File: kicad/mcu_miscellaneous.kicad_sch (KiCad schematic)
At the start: 10 parts, among them SW1 SW_Push, SW2 SW_Push

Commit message: fix(schematic): misc. fixes and stuff - sort all sheets - add the author's name to all sheets and update the date - add 0R resistor to the input of each crystal oscillator - reannotate all symbols - remove todo.md
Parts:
- renumbered C17 to C16, C16 to C17, D3 to D2, R7 to R3, R2 to R4, R1 to R5, R9 to R6
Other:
- moved on the sheet: C16, C17, D1, D2, R3, R4, R5, R6, SW1, SW2

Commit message: everything: select real components, refactor schematic, add a user-led driving circuit, and more
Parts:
- added Q1: NPN, symbol Simulation_SPICE:NPN
- added R13, R16: 5k1, Resistor_SMD:R_0402_1005Metric, symbol Device:R
- C16, C17: footprint (none) -> Capacitor_SMD:C_0402_1005Metric; Distributor (none) -> LCSC; Distributor Link (none) -> https://www.lcsc.com/product-detail/C60474.html?s_z=s_p_CC0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; MPN (none) -> CC0402KRX7R7BB104; Manufacturer (none) -> YAGEO
- D1: footprint (none) -> LED_SMD:LED_0402_1005Metric; Distributor (none) -> LCSC; Distributor Link (none) -> https://www.lcsc.com/product-detail/C511042.html?s_z=s_p_VL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; MPN (none) -> VLMB1500-GS08; Manufacturer (none) -> VISHAY
- D2: Distributor (none) -> LCSC; MPN (none) -> BAT54KFILM; Manufacturer Part Number BAT54KFILM -> (none)
- R3: value 220R -> 0R; footprint (none) -> Resistor_SMD:R_0402_1005Metric
- R4, R5, R6: footprint (none) -> Resistor_SMD:R_0402_1005Metric
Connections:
- net +3V3: now also D1.2 (A)
- net GND: now also Q1.3 (E), R16.1; no longer R3.2
- net USER_LED: now also R13.1; no longer D1.2 (A)
- new net: Q1.1 (C), R3.2
- new net: Q1.2 (B), R13.2, R16.2
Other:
- note added: "Blue LED, Has a high V_F. and 3V3 will let about 10 mA of current. and my STM32 won't like that."
- note added: "maybe this can act as a fuse?"
- note added: "this is placed to prevent leakage current from turning the transistor on spontaneously. similar to MOSFETs I guess.... But I think I need to make it a bit smaller, not very small though, or the NPN wont turn on. Making it smaller in LTSpice (2N2222) to around 500 ohms made it unable to achieve saturation. and the resistor will also conduct too much current. so, if not carefully, this is a double 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"
- moved on the sheet: C16, C17, D1, D2, R3, R4, R5, R6, SW1, SW2

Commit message: feat(components): add details
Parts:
- D1: value LED -> VLMB1500-GS08
- SW1, SW2: value SW_Push -> B3U-1000P; Distributor (none) -> LCSC; Distributor Link (none) -> https://www.lcsc.com/product-detail/C231329.html?spm=wm.fly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; MPN (none) -> B3U-1000P; Manufacturer (none) -> OMRON
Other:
- note added: "verify footprint"
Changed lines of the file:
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@@
+		)
+	)
+	(text "verify footprint"
+		(exclude_from_sim no)
+		(at 110.49 115.57 0)
+		(effects
+			(font
+				(size 1.27 1.27)
+			)
 		)
 	)
@@
 			)
 		)
-		(property "Value" "SW_Push"
+		(property "Value" "B3U-1000P"
 			(at 162.56 99.0599 90)
 			(show_name no)
@@
 			)
 		)
-		(property "Datasheet" ""
+		(property "Datasheet" "https://www.lcsc.com/datasheet/C231329.pdf?spm=wm.sxq.inf.ggs___wm.fly.bg.2.xh&lcsc_vid=RlRYUFFURFcNVFIDFVMMXgZSRlJeUABSQVNfAwJfQwIxVlNeTlZeVlJfTlNaVDtW"
 			(at 156.21 97.79 0)
 			(hide yes)
@@
 			)
 		)
-		(property "Description" "Push button switch, generic, two pins"
+		(property "Description" "SWITCH TACTILE SPST 153gf SMD"
 			(at 161.29 97.79 0)
 			(hide yes)
@@
 			)
 		)
-		(property "Distributor Link" ""
+		(property "Distributor Link" "https://www.lcsc.com/product-detail/C231329.html?spm=wm.fly.bg.2.xh___wm.fly.tp.20.ml&lcsc_vid=RlRYUFFURFcNVFIDFVMMXgZSRlJeUABSQVNfAwJfQwIxVlNeTlZeVlJfTlNaVDtW"
 			(at 161.29 97.79 90)
 			(hide yes)
@@
 			)
 		)
-		(property "Manufacturer" ""
+		(property "Manufacturer" "OMRON"
 			(at 161.29 97.79 90)
 			(hide yes)
@@
 			)
 		)
-		(property "Distributor" ""
+		(property "Distributor" "LCSC"
+			(at 161.29 97.79 90)
+			(hide yes)
+			(show_name no)
+			(do_not_autoplace no)
+			(effects
+				(font
+					(size 1.27 1.27)
+				)
+			)
+		)
+		(property "MPN" "B3U-1000P"
 			(at 161.29 97.79 90)
 			(hide yes)
@@
 			)
 		)
-		(property "Value" "SW_Push"
+		(property "Value" "B3U-1000P"
 			(at 217.17 110.4899 90)
 			(show_name no)
@@
 			)
 		)
-		(property "Datasheet" ""
+		(property "Datasheet" "https://www.lcsc.com/datasheet/C231329.pdf?spm=wm.sxq.inf.ggs___wm.fly.bg.2.xh&lcsc_vid=RlRYUFFURFcNVFIDFVMMXgZSRlJeUABSQVNfAwJfQwIxVlNeTlZeVlJfTlNaVDtW"
 			(at 210.82 109.22 0)
 			(hide yes)
@@
 			)
 		)
-		(property "Description" "Push button switch, generic, two pins"
+		(property "Description" "SWITCH TACTILE SPST 153gf SMD"
 			(at 215.9 109.22 0)
 			(hide yes)
@@
 			)
 		)
-		(property "Distributor Link" ""
+		(property "Distributor Link" "https://www.lcsc.com/product-detail/C231329.html?spm=wm.fly.bg.2.xh___wm.fly.tp.20.ml&lcsc_vid=RlRYUFFURFcNVFIDFVMMXgZSRlJeUABSQVNfAwJfQwIxVlNeTlZeVlJfTlNaVDtW"
 			(at 215.9 109.22 90)
 			(hide yes)
@@
 			)
 		)
-		(property "Manufacturer" ""
+		(property "Manufacturer" "OMRON"
 			(at 215.9 109.22 90)
 			(hide yes)
@@
 			)
 		)
-		(property "Distributor" ""
+		(property "Distributor" "LCSC"
+			(at 215.9 109.22 90)
+			(hide yes)
+			(show_name no)
+			(do_not_autoplace no)
+			(effects
+				(font
+					(size 1.27 1.27)
+				)
+			)
+		)
+		(property "MPN" "B3U-1000P"
 			(at 215.9 109.22 90)
 			(hide yes)
@@
 			)
 		)
-		(property "Value" "LED"
+		(property "Value" "VLMB1500-GS08"
 			(at 99.06 87.9474 90)
 			(show_name no)

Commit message: fix(footprints and symbols): add missing footprints and symbols
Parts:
- removed Q1: NPN, symbol Simulation_SPICE:NPN
- removed SW1, SW2: B3U-1000P, symbol Switch:SW_Push
- added Q1: S9013-E, Package_TO_SOT_SMD:SOT-23, symbol #stm32-bt-board-external-symbols:S9013-E
- added SW1, SW2: B3U-1000P, #stm32-bt-board-external-footprints:B3U-1000P, symbol #stm32-bt-board-external-symbols:B3U-1000P
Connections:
- net +3V3: now also SW1.2
- net GND: now also Q1.2 (E), SW2.1
- net NRST_IN: now also SW2.2
- net at R3.2: now also Q1.3 (C)
- net at R13.2, R16.2: now also Q1.1 (B)
- net at R4.1: now also SW1.1
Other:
- note removed: "verify footprint"

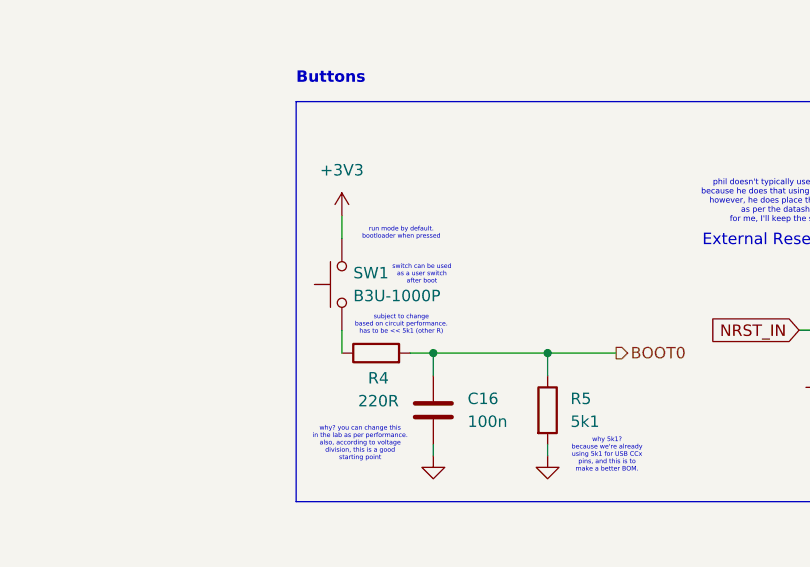
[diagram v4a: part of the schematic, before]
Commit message: refactor(schematic): flip SW1 so layout is nicer
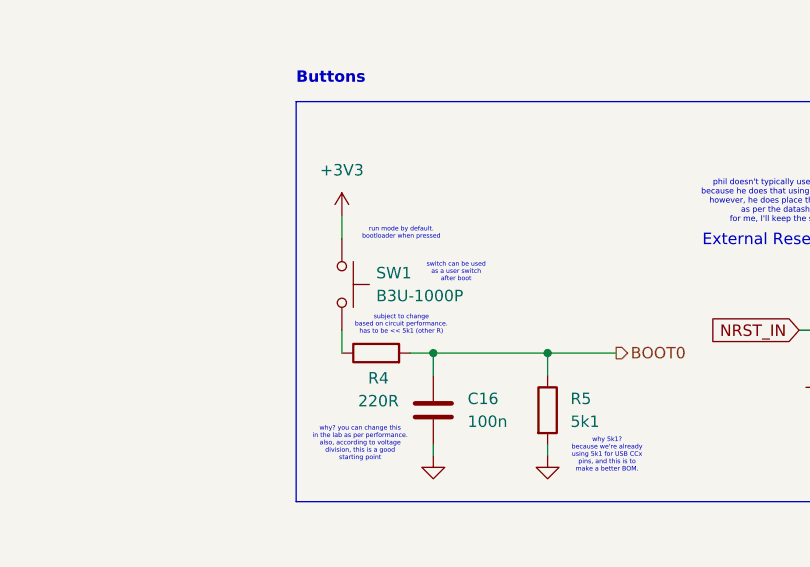
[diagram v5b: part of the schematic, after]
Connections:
- net +3V3: now also SW1.1; no longer SW1.2
- net at R4.1: now also SW1.2; no longer SW1.1
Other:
- moved on the sheet: SW1
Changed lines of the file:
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@@
 	(text "switch can be used\nas a user switch\nafter boot"
 		(exclude_from_sim no)
-		(at 170.18 96.774 0)
+		(at 173.99 96.52 0)
 		(effects
 			(font
@@
 	(symbol
 		(lib_id "#stm32-bt-board-external-symbols:B3U-1000P")
-		(at 161.29 97.79 90)
+		(at 161.29 97.79 270)
 		(unit 1)
 		(body_style 1)
@@
 		(fields_autoplaced yes)
 		(property "Reference" "SW1"
-			(at 162.56 96.5199 90)
-			(show_name no)
-			(do_not_autoplace no)
-			(effects
-				(font
-					(size 1.27 1.27)
-				)
-				(justify right)
+			(at 165.1 96.5199 90)
+			(show_name no)
+			(do_not_autoplace no)
+			(effects
+				(font
+					(size 1.27 1.27)
+				)
+				(justify left)
 			)
 		)
 		(property "Value" "B3U-1000P"
-			(at 162.56 99.0599 90)
-			(show_name no)
-			(do_not_autoplace no)
-			(effects
-				(font
-					(size 1.27 1.27)
-				)
-				(justify right)
+			(at 165.1 99.0599 90)
+			(show_name no)
+			(do_not_autoplace no)
+			(effects
+				(font
+					(size 1.27 1.27)
+				)
+				(justify left)
 			)
 		)
 		(property "Footprint" "#stm32-bt-board-external-footprints:B3U-1000P"
-			(at 156.21 97.79 0)
+			(at 166.37 97.79 0)
 			(hide yes)
 			(show_name no)
@@
 		)
 		(property "Datasheet" "https://www.lcsc.com/datasheet/C231329.pdf?spm=wm.sxq.inf.ggs___wm.fly.bg.0.xh&lcsc_vid=RlRYUFFURFcNVFIDFVMMXgZSRlJeUABSQVNfAwJfQwIxVlNeTllXUlNQR1dcUzsOAxUeFF5JWBYZEEoKFBINSQcJGk4eFQsCAgIaSgADAwAHC0slRFBXUFJeQ08GEwkK"
-			(at 156.21 97.79 0)
-			(hide yes)
-			(show_name no)
+			(at 166.37 97.79 0)
+			(hide yes)
+			(show_name no)

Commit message: feat(BOM): fill missing parts in BOM
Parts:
- R13, R16, R5: Distributor (none) -> LCSC; Distributor Link (none) -> https://www.lcsc.com/product-detail/C105872.html; MPN (none) -> RC0402FR-075K1L; Manufacturer (none) -> YAGEO
- R3: Distributor (none) -> LCSC; Distributor Link (none) -> https://www.lcsc.com/product-detail/C190119.html; MPN (none) -> CRCW04020000Z0ED; Manufacturer (none) -> VISHAY
- R4: Distributor (none) -> LCSC; Distributor Link (none) -> https://www.lcsc.com/product-detail/C2909336.html; MPN (none) -> FRC0402F2200TS; Manufacturer (none) -> FOJAN
- R6: Distributor (none) -> LCSC; Distributor Link (none) -> https://www.lcsc.com/product-detail/C60491.html; MPN (none) -> RC0402FR-07100KL; Manufacturer (none) -> YAGEO
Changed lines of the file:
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@@
 			)
 		)
-		(property "Datasheet" ""
+		(property "Datasheet" "https://www.lcsc.com/datasheet/C105872.pdf"
 			(at 184.15 111.76 0)
 			(hide yes)
@@
 			)
 		)
-		(property "Description" "-- mixed values --"
+		(property "Description" "RES 5.1kΩ ±1% 62.5mW 0402"
 			(at 184.15 111.76 0)
 			(hide yes)
@@
 			)
 		)
-		(property "Distributor Link" ""
+		(property "Distributor Link" "https://www.lcsc.com/product-detail/C105872.html"
 			(at 184.15 111.76 0)
 			(hide yes)
@@
 			)
 		)
-		(property "Manufacturer" ""
+		(property "Manufacturer" "YAGEO"
 			(at 184.15 111.76 0)
 			(hide yes)
@@
 			)
 		)
-		(property "Distributor" ""
+		(property "Distributor" "LCSC"
+			(at 184.15 111.76 0)
+			(hide yes)
+			(show_name no)
+			(do_not_autoplace no)
+			(effects
+				(font
+					(size 1.27 1.27)
+				)
+			)
+		)
+		(property "MPN" "RC0402FR-075K1L"
 			(at 184.15 111.76 0)
 			(hide yes)
@@
 			)
 		)
-		(property "Datasheet" ""
+		(property "Datasheet" "https://www.lcsc.com/datasheet/C105872.pdf"
 			(at 83.82 121.92 0)
 			(hide yes)
@@
 			)
 		)
-		(property "Description" "Resistor"
+		(property "Description" "RES 5.1kΩ ±1% 62.5mW 0402"
+			(at 83.82 121.92 0)
+			(hide yes)
+			(show_name no)
+			(do_not_autoplace no)
+			(effects
+				(font
+					(size 1.27 1.27)
+				)
+			)
+		)
+		(property "Distributor" "LCSC"
+			(at 83.82 121.92 0)
+			(hide yes)
+			(show_name no)
+			(do_not_autoplace no)
+			(effects
+				(font
+					(size 1.27 1.27)
+				)
+			)
+		)
+		(property "Distributor Link" "https://www.lcsc.com/product-detail/C105872.html"
+			(at 83.82 121.92 0)
+			(hide yes)
+			(show_name no)
+			(do_not_autoplace no)
+			(effects
+				(font
+					(size 1.27 1.27)
+				)
+			)
+		)
+		(property "MPN" "RC0402FR-075K1L"
+			(at 83.82 121.92 0)
+			(hide yes)
+			(show_name no)
+			(do_not_autoplace no)
+			(effects
+				(font
+					(size 1.27 1.27)
+				)
+			)
+		)
+		(property "Manufacturer" "YAGEO"
 			(at 83.82 121.92 0)
 			(hide yes)
@@
 			)
 		)
-		(property "Datasheet" ""
+		(property "Datasheet" "https://www.lcsc.com/datasheet/C190119.pdf"
 			(at 95.25 104.14 0)
 			(hide yes)
@@
 			)
 		)
-		(property "Description" "Resistor"
+		(property "Description" "RES 0Ω 62.5mW 0402"
 			(at 95.25 104.14 0)
 			(hide yes)
@@
 			)
 		)
-		(property "Distributor Link" ""
+		(property "Distributor Link" "https://www.lcsc.com/product-detail/C190119.html"
 			(at 95.25 104.14 0)
 			(hide yes)
@@
 			)
 		)
-		(property "Manufacturer" ""
+		(property "Manufacturer" "VISHAY"
 			(at 95.25 104.14 0)
 			(hide yes)
@@
 			)
 		)
-		(property "Distributor" ""
+		(property "Distributor" "LCSC"
+			(at 95.25 104.14 0)
+			(hide yes)
+			(show_name no)
+			(do_not_autoplace no)
+			(effects
+				(font
+					(size 1.27 1.27)
+				)
+			)
+		)
+		(property "MPN" "CRCW04020000Z0ED"
 			(at 95.25 104.14 0)
 			(hide yes)
@@
 			)
 		)
-		(property "Datasheet" ""
+		(property "Datasheet" "https://www.lcsc.com/datasheet/C2909336.pdf"
 			(at 165.1 105.41 0)
 			(hide yes)
@@
 			)
 		)
-		(property "Description" "Resistor"
+		(property "Description" "RES 220Ω ±1% 62.5mW 0402"
 			(at 165.1 105.41 0)
 			(hide yes)
@@
 			)
 		)
-		(property "Distributor Link" ""
+		(property "Distributor Link" "https://www.lcsc.com/product-detail/C2909336.html"
 			(at 165.1 105.41 90)
 			(hide yes)
@@
 			)
 		)
-		(property "Manufacturer" ""
+		(property "Manufacturer" "FOJAN"
 			(at 165.1 105.41 90)
 			(hide yes)
@@
 			)
 		)
-		(property "Distributor" ""
+		(property "Distributor" "LCSC"
+			(at 165.1 105.41 90)
+			(hide yes)
+			(show_name no)
+			(do_not_autoplace no)
+			(effects
+				(font
+					(size 1.27 1.27)
+				)
+			)
+		)
+		(property "MPN" "FRC0402F2200TS"
 			(at 165.1 105.41 90)
 			(hide yes)
@@
 			)
 		)
-		(property "Datasheet" ""
+		(property "Datasheet" "https://www.lcsc.com/datasheet/C60491.pdf"
 			(at 250.19 96.52 0)
 			(hide yes)
@@
 			)
 		)
-		(property "Description" "Resistor"
+		(property "Description" "RES 100kΩ ±1% 62.5mW 0402"
 			(at 250.19 96.52 0)
 			(hide yes)
@@
 			)
 		)
-		(property "Distributor" ""
+		(property "Distributor" "LCSC"
+			(at 250.19 96.52 0)
+			(hide yes)
+			(show_name no)
+			(do_not_autoplace no)
+			(effects
+				(font
+					(size 1.27 1.27)
+				)
+			)
+		)
+		(property "Distributor Link" "https://www.lcsc.com/product-detail/C60491.html"
+			(at 250.19 96.52 0)
+			(hide yes)
+			(show_name no)
+			(do_not_autoplace no)
+			(effects
+				(font
+					(size 1.27 1.27)
+				)
+			)
+		)
+		(property "MPN" "RC0402FR-07100KL"
+			(at 250.19 96.52 0)
+			(hide yes)
+			(show_name no)
+			(do_not_autoplace no)
+			(effects
+				(font
+					(size 1.27 1.27)
+				)
+			)
+		)
+		(property "Manufacturer" "YAGEO"
 			(at 250.19 96.52 0)
 			(hide yes)
@@
 			)
 		)
-		(property "Datasheet" ""
+		(property "Datasheet" "https://www.lcsc.com/datasheet/C105872.pdf"
 			(at 73.66 115.57 0)
 			(hide yes)
@@
 			)
 		)
-		(property "Description" "Resistor"
+		(property "Description" "RES 5.1kΩ ±1% 62.5mW 0402"
 			(at 73.66 115.57 0)
 			(hide yes)
 			(show_name no)
+			(do_not_autoplace no)
+			(effects
+				(font
+					(size 1.27 1.27)
+				)
+			)
+		)
+		(property "Distributor" "LCSC"
+			(at 73.66 115.57 90)
+			(hide yes)
+			(show_name no)
+			(do_not_autoplace no)
+			(effects
+				(font
+					(size 1.27 1.27)
+				)
+			)
+		)
+		(property "Distributor Link" "https://www.lcsc.com/product-detail/C105872.html"
+			(at 73.66 115.57 90)
+			(hide yes)
+			(show_name no)
+			(do_not_autoplace no)
+			(effects
+				(font
+					(size 1.27 1.27)
+				)
+			)
+		)
+		(property "MPN" "RC0402FR-075K1L"
+			(at 73.66 115.57 90)
+			(hide yes)
+			(show_name no)
+			(do_not_autoplace no)
+			(effects
+				(font
+					(size 1.27 1.27)
+				)
+			)
+		)
+		(property "Manufacturer" "YAGEO"
+			(at 73.66 115.57 90)
+			(hide yes)
+			(show_name no)

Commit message: feat(manuf.): edit BOM and CPL to match JLCPCB's requirements
however, please pay close attention to the rotations during ordering, especially for the SOT components, as JLCPCB messes them up a bit, same for the connector and the filter
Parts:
- C16, C17: Distributor Link https://www.lcsc.com/product-detail/C60474.html?s_z=s_p_CC0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 -> https://www.lcsc.com/product-detail/C60474.html; JLCPCB Part # (none) -> C60474
- D1: Distributor Link https://www.lcsc.com/product-detail/C511042.html?s_z=s_p_VL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 -> https://www.lcsc.com/product-detail/C511042.html; JLCPCB Part # (none) -> C511042
- D2: Distributor Link https://www.lcsc.com/product-detail/C283259.html?s_z=s_p_BA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 -> https://www.lcsc.com/product-detail/C283259.html; JLCPCB Part # (none) -> C283259
- Q1: Distributor Link https://www.lcsc.com/product-detail/C41371419.html?s_z=h_q_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 -> https://www.lcsc.com/product-detail/C41371419.html; JLCPCB Part # (none) -> C41371419
- R13, R16, R5: JLCPCB Part # (none) -> C105872
- R3: JLCPCB Part # (none) -> C190119
- R4: JLCPCB Part # (none) -> C2909336
- R6: JLCPCB Part # (none) -> C60491
- SW1, SW2: Distributor Link https://www.lcsc.com/product-detail/C231329.html?s_z=n_q_b3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 -> https://www.lcsc.com/product-detail/C231329.html; JLCPCB Part # (none) -> C231329
